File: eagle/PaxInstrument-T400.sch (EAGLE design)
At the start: 131 parts, among them IC1 MCP3424, IC3 SN74LVC1G74DCT, J1 MICRO-SDCARD-CONNECTOR-330006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, Q1 DMP2035U-7, Q2 DMP2035U-7, Q3 DMN2075U-7, Q4 DMN2075U-7, Q5 DMP2035U-7, U1 MCP9800, U2 APX809, U3 MCP73831, U4 MIC5219-3.3V, X1 FH12-12S-1S, Y1 RESONATORSMD

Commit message: Updated TC connector
Changed Keystone connector to thermo-Clip2 designed by Pax instrument.
(Thermocouple connector placement #179)
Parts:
- U$10, U$11, U$12, U$13: value CHARLESPAX_TC-MINI-CONNECTOR -> TC-MINI-OUTSIDE; device PaxInstrument-T400:CHARLESPAX_TC-MINI-CONNECTOR -> PaxInstruments-Connectors:TC-MINI-OUTSIDE; MF Keystone -> Pax Instrument; MPN 3572 -> Thermo-clip2
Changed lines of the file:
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@@
 <attribute name="MPN" value="N/A"/>
 </part>
-<part name="U$10" library="PaxInstrument-T400" deviceset="CHARLESPAX_TC-MINI-CONNECTOR" device="">
-<attribute name="MF" value="Keystone"/>
-<attribute name="MPN" value="3572"/>
+<part name="U$10" library="PaxInstruments-Connectors" deviceset="TC-MINI-OUTSIDE" device="">
+<attribute name="MF" value="Pax Instrument"/>
+<attribute name="MPN" value="Thermo-clip2"/>
 </part>
-<part name="U$11" library="PaxInstrument-T400" deviceset="CHARLESPAX_TC-MINI-CONNECTOR" device="">
-<attribute name="MF" value="Keystone"/>
-<attribute name="MPN" value="3572"/>
+<part name="U$11" library="PaxInstruments-Connectors" deviceset="TC-MINI-OUTSIDE" device="">
+<attribute name="MF" value="Pax Instrument"/>
+<attribute name="MPN" value="Thermo-clip2"/>
 </part>
-<part name="U$12" library="PaxInstrument-T400" deviceset="CHARLESPAX_TC-MINI-CONNECTOR" device="">
-<attribute name="MF" value="Keystone"/>
-<attribute name="MPN" value="3572"/>
+<part name="U$12" library="PaxInstruments-Connectors" deviceset="TC-MINI-OUTSIDE" device="">
+<attribute name="MF" value="Pax Instrument"/>
+<attribute name="MPN" value="Thermo-clip2"/>
 </part>
-<part name="U$13" library="PaxInstrument-T400" deviceset="CHARLESPAX_TC-MINI-CONNECTOR" device="">
-<attribute name="MF" value="Keystone"/>
-<attribute name="MPN" value="3572"/>
+<part name="U$13" library="PaxInstruments-Connectors" deviceset="TC-MINI-OUTSIDE" device="">
+<attribute name="MF" value="Pax Instrument"/>
+<attribute name="MPN" value="Thermo-clip2"/>
 </part>
 <part name="GND18" library="SparkFun-Aesthetics" deviceset="GND" device=""/>

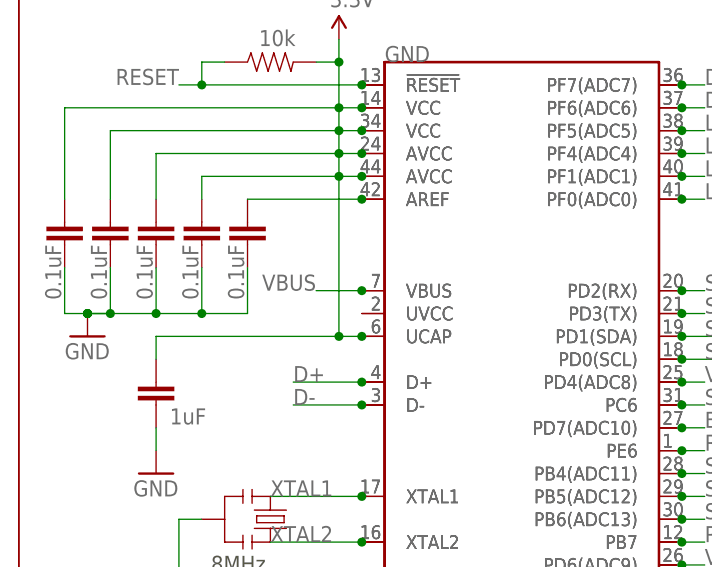
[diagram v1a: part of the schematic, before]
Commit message: Connect MCU VBUS pin to USB connector - VBUS_IN #183
Updated schematic and it allows firmware using VBUS pin on MCU to detect
USB power supply connection status.
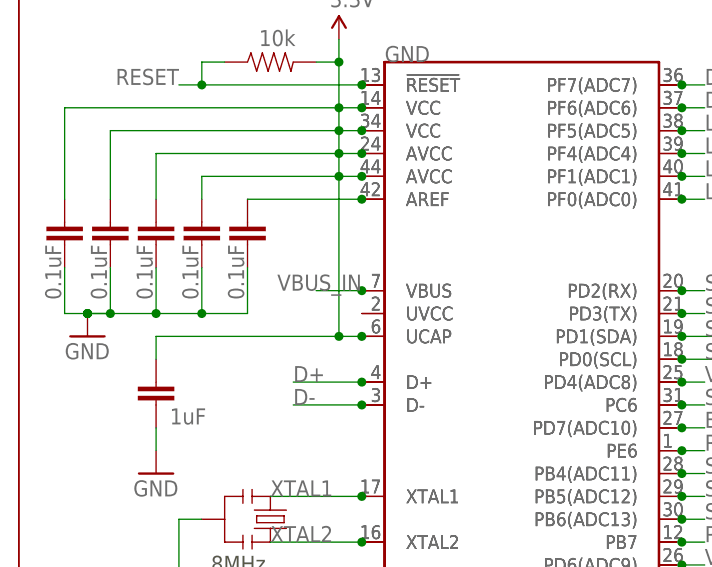
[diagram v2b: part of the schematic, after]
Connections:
- net VBUS: no longer GND.VBUS, U$3.VBUS
- net VBUS_IN: now also GND.VBUS, U$3.VBUS
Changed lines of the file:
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@@
 <junction x="292.1" y="246.38"/>
-</segment>
-<segment>
-<label x="40.64" y="152.4" size="1.778" layer="95" rot="MR0"/>
-<wire x1="45.72" y1="152.4" x2="40.64" y2="152.4" width="0.1524" layer="91"/>
-<pinref part="GND" gate="G$1" pin="VBUS"/>
-<pinref part="U$3" gate="G$1" pin="VBUS"/>
-<junction x="45.72" y="152.4"/>
 </segment>
 </net>
@@
 <wire x1="27.94" y1="246.38" x2="68.58" y2="246.38" width="0.1524" layer="91"/>
 </segment>
-</net>
+<segment>
+<label x="45.72" y="152.4" size="1.778" layer="95" rot="MR0"/>
+<wire x1="45.72" y1="152.4" x2="40.64" y2="152.4" width="0.1524" layer="91"/>
+<pinref part="GND" gate="G$1" pin="VBUS"/>
+<pinref part="U$3" gate="G$1" pin="VBUS"/>
+<junction x="45.72" y="152.4"/>
+</segment>
+</net>

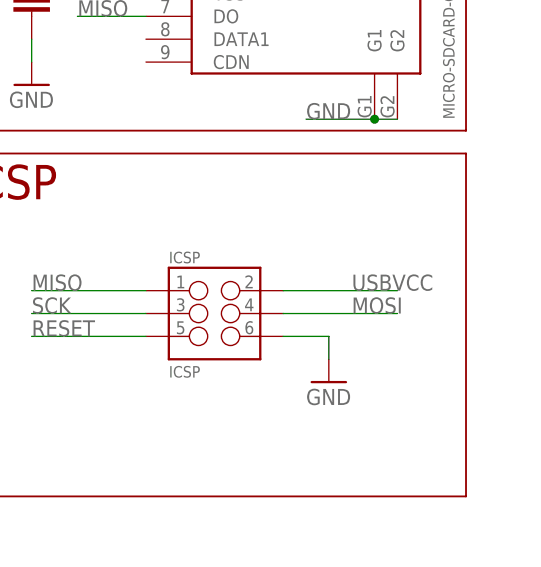
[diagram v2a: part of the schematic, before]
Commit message: Updated PCB and Schematic
-Thermocouple connector placement #179
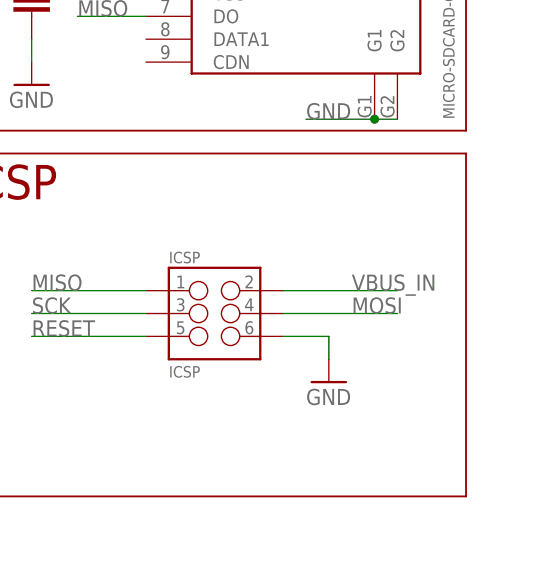
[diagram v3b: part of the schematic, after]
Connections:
- removed net USBVCC: ICSP.2
- net VBUS_IN: now also ICSP.2
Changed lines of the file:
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@@
-</segment>
-</net>
-<net name="USBVCC" class="1">
-<segment>
-<pinref part="ICSP" gate="G$1" pin="2"/>
-<wire x1="355.6" y1="96.52" x2="368.3" y2="96.52" width="0.1524" layer="91"/>
-<label x="363.22" y="96.52" size="1.778" layer="95"/>
 </segment>
 </net>
@@
 <junction x="45.72" y="152.4"/>
 </segment>
-</net>
+<segment>
+<pinref part="ICSP" gate="G$1" pin="2"/>
+<wire x1="355.6" y1="96.52" x2="368.3" y2="96.52" width="0.1524" layer="91"/>
+<label x="363.22" y="96.52" size="1.778" layer="95"/>
+</segment>
+</net>

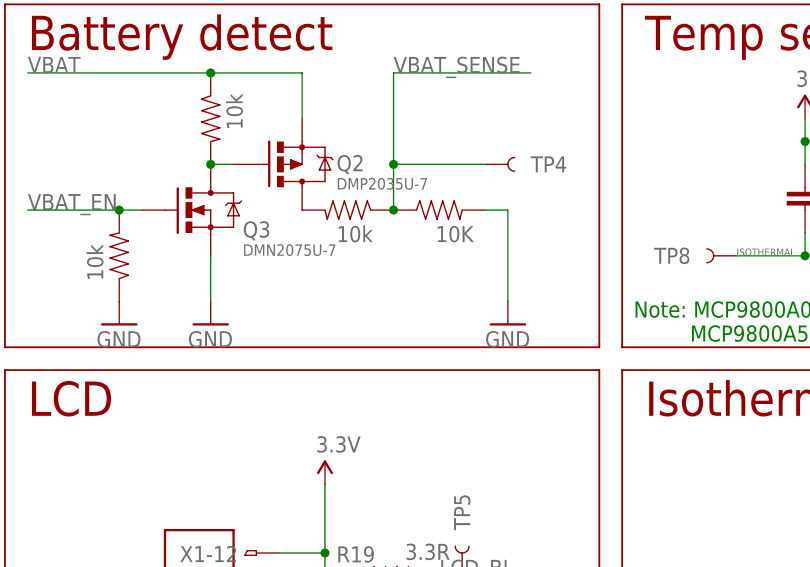
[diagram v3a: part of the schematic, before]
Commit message: Updated battery detect circuit in Sch and PCB layout
- Internal analog reference voltage #156
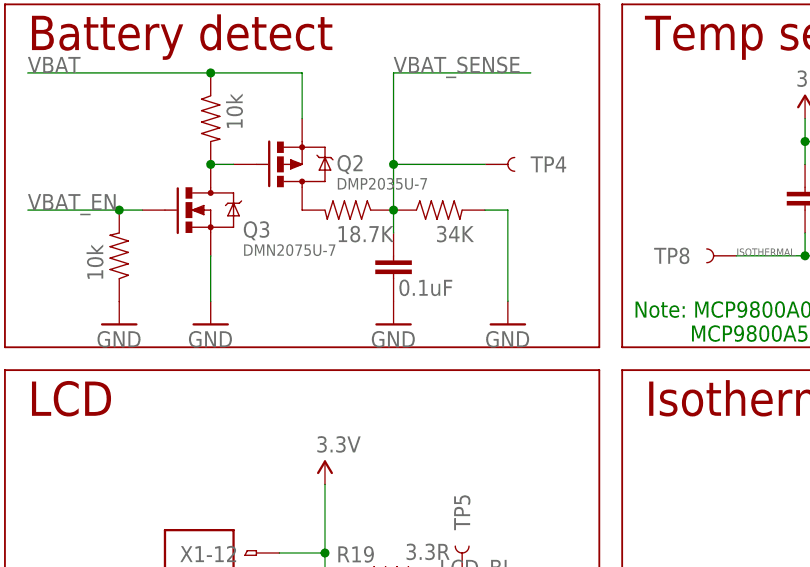
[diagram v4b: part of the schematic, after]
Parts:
- added C23: 0.1uF, PaxInstrument-T400:SPARKFUN-CAPACITORS_CAP0603-CAP
- R20: value 10k -> 18.7K
- R24: value 10K -> 34K
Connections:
- net GND: now also C23.2
- net VBAT_SENSE: now also C23.1
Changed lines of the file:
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@@
 <attribute name="MPN" value="95278-101A06LF"/>
 </part>
-<part name="R20" library="PaxInstrument-T400" deviceset="SPARKFUN-RESISTORS_RESISTOR" device="0603-RES" value="10k">
+<part name="R20" library="PaxInstrument-T400" deviceset="SPARKFUN-RESISTORS_RESISTOR" device="0603-RES" value="18.7K">
 <attribute name="MPN" value=""/>
 </part>
@@
 <attribute name="MPN" value="MBR230S1F-7"/>
 </part>
-<part name="R24" library="PaxInstrument-T400" deviceset="SPARKFUN-RESISTORS_RESISTOR" device="0603-RES" value="10K">
+<part name="R24" library="PaxInstrument-T400" deviceset="SPARKFUN-RESISTORS_RESISTOR" device="0603-RES" value="34K">
 <attribute name="MPN" value=""/>
 </part>
@@
 <part name="GND21" library="SparkFun-Aesthetics" deviceset="GND" device=""/>
 <part name="GND35" library="SparkFun-Aesthetics" deviceset="GND" device=""/>
+<part name="C23" library="PaxInstrument-T400" deviceset="SPARKFUN-CAPACITORS_CAP" device="0603-CAP" value="0.1uF">
+<attribute name="MPN" value=""/>
+</part>
+<part name="GND36" library="SparkFun-Aesthetics" deviceset="GND" device=""/>
 </parts>
 <sheets>
@@
 <instance part="GND21" gate="1" x="139.7" y="157.48"/>
 <instance part="GND35" gate="1" x="248.92" y="218.44"/>
+<instance part="C23" gate="G$1" x="170.18" y="162.56" smashed="yes">
+<attribute name="VALUE" x="170.688" y="160.655" size="1.778" layer="96"/>
+<attribute name="MPN" x="170.18" y="162.56" size="1.778" layer="96" display="off"/>
+</instance>
+<instance part="GND36" gate="1" x="170.18" y="157.48"/>
 </instances>
 <busses>
@@
 <junction x="248.92" y="220.98"/>
 </segment>
+<segment>
+<pinref part="C23" gate="G$1" pin="2"/>
+<pinref part="GND36" gate="1" pin="GND"/>
+</segment>
 </net>
 <net name="D-" class="0">
@@
 <wire x1="170.18" y1="185.42" x2="185.42" y2="185.42" width="0.1524" layer="91"/>
 <label x="170.18" y="185.42" size="1.778" layer="95"/>
-</segment>
-<segment>
+<pinref part="C23" gate="G$1" pin="1"/>
+<wire x1="170.18" y1="167.64" x2="170.18" y2="170.18" width="0.1524" layer="91"/>
+</segment>
+<segment>

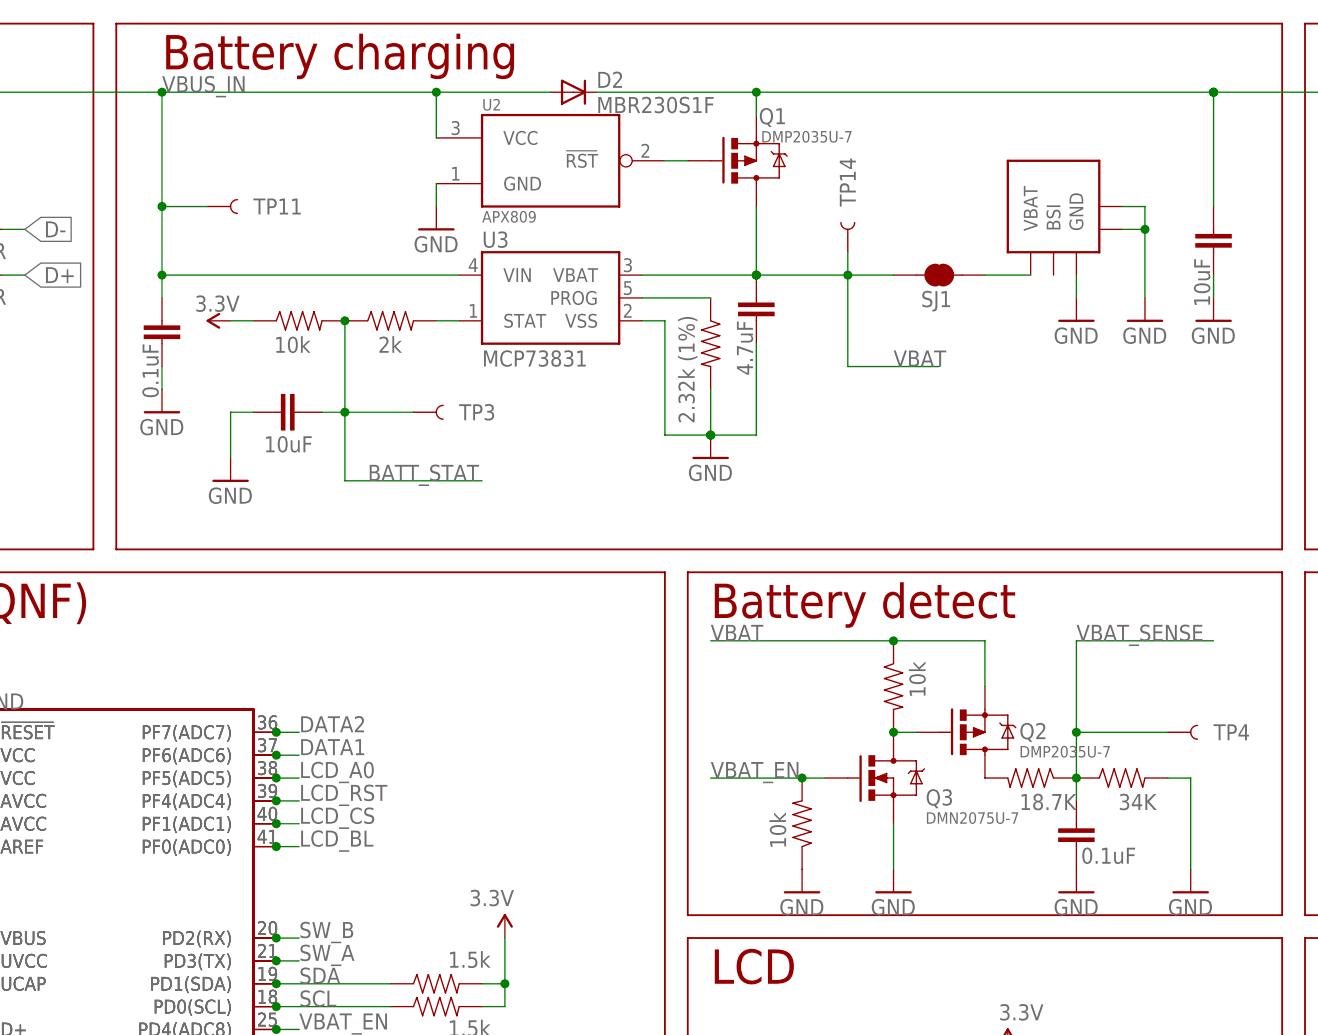
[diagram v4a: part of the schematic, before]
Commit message: updated schematic
- Add 4.7k pulldown to VBUS input #188
- Internal analog reference voltage #156
- DPN pull-up resisors #191
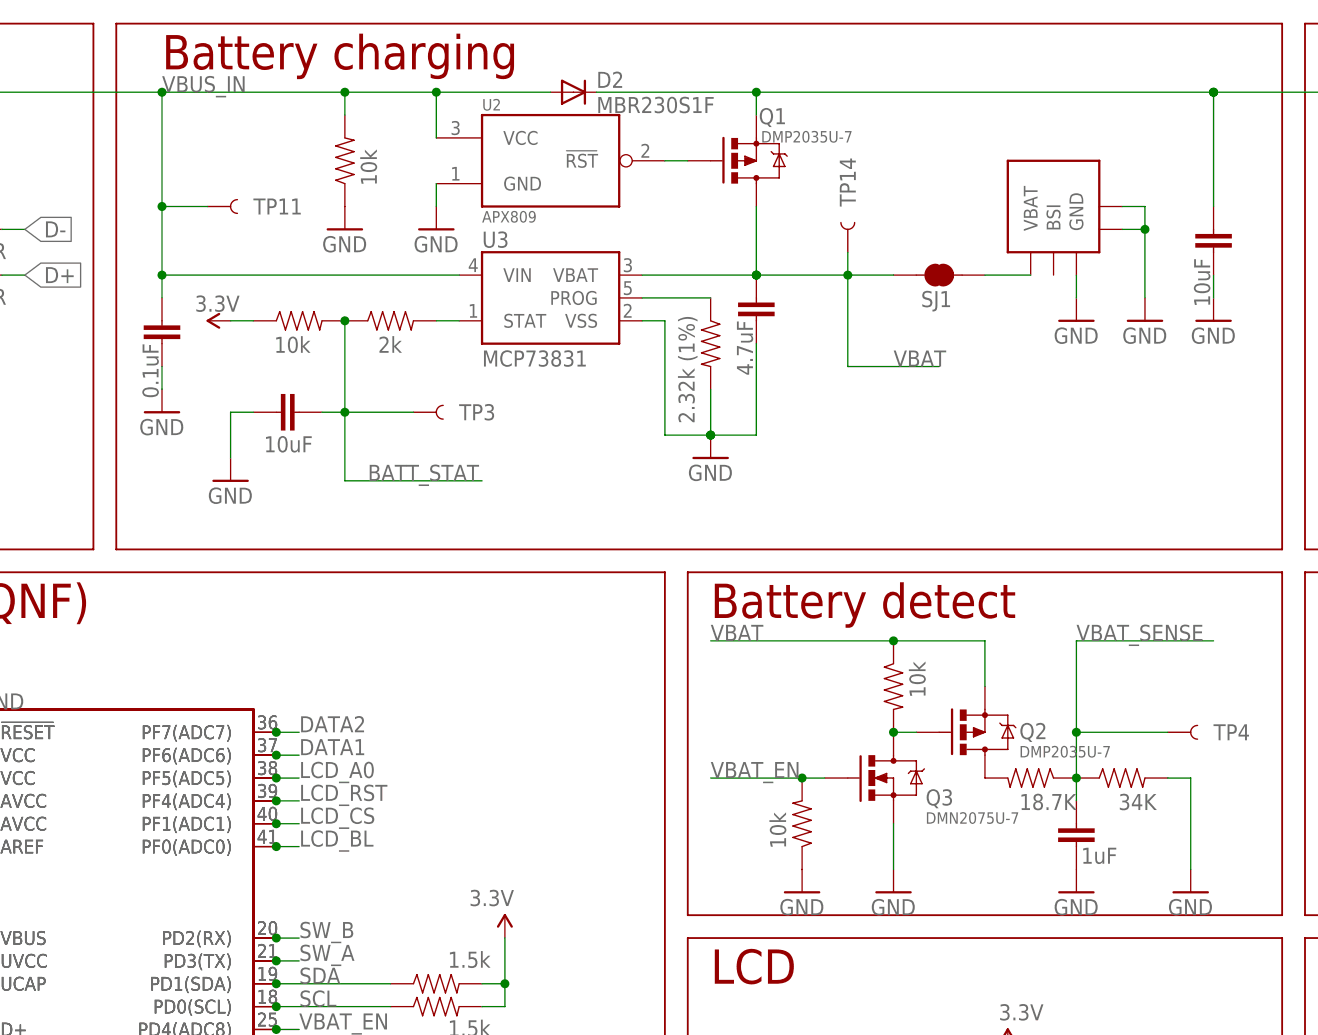
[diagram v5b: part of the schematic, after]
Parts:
- added R25: 10k, PaxInstrument-T400:SPARKFUN-RESISTORS_RESISTOR0603-RES
- C23: value 0.1uF -> 1uF
- R11, R12, R15, R16, R8: POPULATE (none) -> DNP
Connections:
- net GND: now also R25.1
- net VBUS_IN: now also R25.2
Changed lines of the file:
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@@
 <?xml version="1.0" encoding="utf-8"?>
 <!DOCTYPE eagle SYSTEM "eagle.dtd">
-<eagle version="7.1.0">
+<eagle version="7.3.0">
 <drawing>
 <settings>
@@
 <part name="R8" library="PaxInstrument-T400" deviceset="SPARKFUN-RESISTORS_RESISTOR" device="0603-RES" value="10k">
 <attribute name="MPN" value=""/>
+<attribute name="POPULATE" value="DNP"/>
 </part>
 <part name="R11" library="PaxInstrument-T400" deviceset="SPARKFUN-RESISTORS_RESISTOR" device="0603-RES" value="10k">
 <attribute name="MPN" value=""/>
+<attribute name="POPULATE" value="DNP"/>
 </part>
 <part name="R12" library="PaxInstrument-T400" deviceset="SPARKFUN-RESISTORS_RESISTOR" device="0603-RES" value="10k">
 <attribute name="MPN" value=""/>
+<attribute name="POPULATE" value="DNP"/>
 </part>
 <part name="R15" library="PaxInstrument-T400" deviceset="SPARKFUN-RESISTORS_RESISTOR" device="0603-RES" value="10k">
 <attribute name="MPN" value=""/>
+<attribute name="POPULATE" value="DNP"/>
 </part>
 <part name="R16" library="PaxInstrument-T400" deviceset="SPARKFUN-RESISTORS_RESISTOR" device="0603-RES" value="10k">
 <attribute name="MPN" value=""/>
+<attribute name="POPULATE" value="DNP"/>
 </part>
 <part name="P+9" library="SparkFun" deviceset="3.3V" device=""/>
@@
 <part name="GND21" library="SparkFun-Aesthetics" deviceset="GND" device=""/>
 <part name="GND35" library="SparkFun-Aesthetics" deviceset="GND" device=""/>
-<part name="C23" library="PaxInstrument-T400" deviceset="SPARKFUN-CAPACITORS_CAP" device="0603-CAP" value="0.1uF">
+<part name="C23" library="PaxInstrument-T400" deviceset="SPARKFUN-CAPACITORS_CAP" device="0603-CAP" value="1uF">
 <attribute name="MPN" value=""/>
 </part>
 <part name="GND36" library="SparkFun-Aesthetics" deviceset="GND" device=""/>
+<part name="R25" library="PaxInstrument-T400" deviceset="SPARKFUN-RESISTORS_RESISTOR" device="0603-RES" value="10k">
+<attribute name="MPN" value=""/>
+</part>
+<part name="GND37" library="SparkFun-Aesthetics" deviceset="GND" device=""/>
 </parts>
 <sheets>
@@
 <attribute name="VALUE" x="244.602" y="57.15" size="1.778" layer="96" rot="R90"/>
 <attribute name="MPN" x="246.38" y="58.42" size="1.778" layer="96" rot="R270" display="off"/>
+<attribute name="POPULATE" x="246.38" y="58.42" size="1.778" layer="96" rot="R270" display="off"/>
 </instance>
 <instance part="R11" gate="G$1" x="251.46" y="58.42" smashed="yes" rot="R270">
 <attribute name="VALUE" x="249.682" y="57.15" size="1.778" layer="96" rot="R90"/>
 <attribute name="MPN" x="251.46" y="58.42" size="1.778" layer="96" rot="R270" display="off"/>
+<attribute name="POPULATE" x="251.46" y="58.42" size="1.778" layer="96" rot="R270" display="off"/>
 </instance>
 <instance part="R12" gate="G$1" x="256.54" y="58.42" smashed="yes" rot="MR270">
 <attribute name="VALUE" x="253.238" y="57.15" size="1.778" layer="96" rot="MR90"/>
 <attribute name="MPN" x="256.54" y="58.42" size="1.778" layer="96" rot="MR270" display="off"/>
+<attribute name="POPULATE" x="256.54" y="58.42" size="1.778" layer="96" rot="MR270" display="off"/>
 </instance>
 <instance part="R15" gate="G$1" x="215.9" y="58.42" smashed="yes" rot="MR270">
 <attribute name="VALUE" x="212.598" y="57.15" size="1.778" layer="96" rot="MR90"/>
 <attribute name="MPN" x="215.9" y="58.42" size="1.778" layer="96" rot="MR270" display="off"/>
+<attribute name="POPULATE" x="215.9" y="58.42" size="1.778" layer="96" rot="MR270" display="off"/>
 </instance>
 <instance part="R16" gate="G$1" x="210.82" y="58.42" smashed="yes" rot="R270">
 <attribute name="VALUE" x="209.042" y="57.15" size="1.778" layer="96" rot="R90"/>
 <attribute name="MPN" x="210.82" y="58.42" size="1.778" layer="96" rot="R270" display="off"/>
+<attribute name="POPULATE" x="210.82" y="58.42" size="1.778" layer="96" rot="R270" display="off"/>
 </instance>
 <instance part="P+9" gate="G$1" x="233.68" y="63.5" rot="MR0"/>
@@
 </instance>
 <instance part="GND36" gate="1" x="170.18" y="157.48"/>
+<instance part="R25" gate="G$1" x="88.9" y="238.76" smashed="yes" rot="R90">
+<attribute name="VALUE" x="90.678" y="240.03" size="1.778" layer="96" rot="R270"/>
+<attribute name="MPN" x="88.9" y="238.76" size="1.778" layer="96" rot="R90" display="off"/>
+</instance>
+<instance part="GND37" gate="1" x="88.9" y="231.14"/>
 </instances>
 <busses>
@@
 <pinref part="GND36" gate="1" pin="GND"/>
 </segment>
+<segment>
+<pinref part="R25" gate="G$1" pin="1"/>
+<pinref part="GND37" gate="1" pin="GND"/>
+</segment>
 </net>
 <net name="D-" class="0">
@@
 <junction x="68.58" y="246.38"/>
 <label x="68.58" y="246.38" size="1.778" layer="95"/>
-<wire x1="99.06" y1="246.38" x2="68.58" y2="246.38" width="0.1524" layer="91"/>
+<wire x1="99.06" y1="246.38" x2="88.9" y2="246.38" width="0.1524" layer="91"/>
 <pinref part="TP11" gate="G$1" pin="1"/>
+<wire x1="88.9" y1="246.38" x2="68.58" y2="246.38" width="0.1524" layer="91"/>
 <wire x1="73.66" y1="233.68" x2="68.58" y2="233.68" width="0.1524" layer="91"/>
 <junction x="68.58" y="233.68"/>
@@
 <wire x1="27.94" y1="231.14" x2="27.94" y2="246.38" width="0.1524" layer="91"/>
 <wire x1="27.94" y1="246.38" x2="68.58" y2="246.38" width="0.1524" layer="91"/>
-</segment>
-<segment>
+<pinref part="R25" gate="G$1" pin="2"/>
+<wire x1="88.9" y1="243.84" x2="88.9" y2="246.38" width="0.1524" layer="91"/>
+<junction x="88.9" y="246.38"/>
+</segment>
+<segment>
